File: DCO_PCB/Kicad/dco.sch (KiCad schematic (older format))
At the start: 0 parts

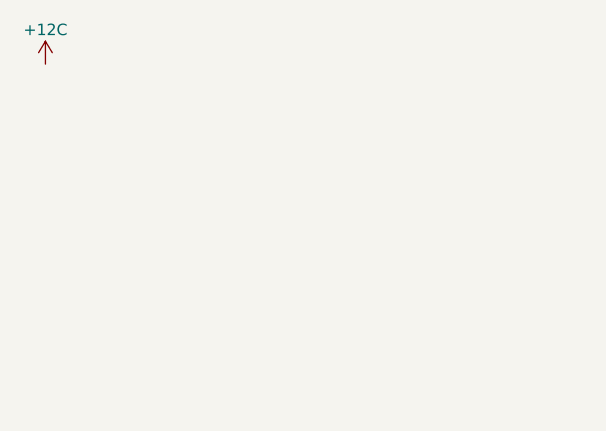
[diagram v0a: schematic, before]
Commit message: s-a adaugat gndd Signed-off-by: Botond Sandor Kirei <botond.kirei@bel.utcluj.ro>
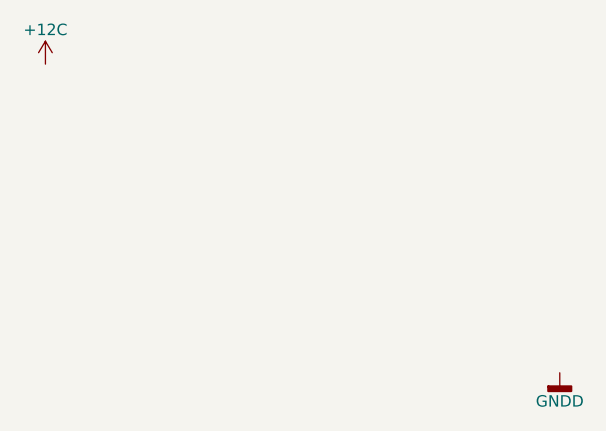
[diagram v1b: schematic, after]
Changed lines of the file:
@@
 LIBS:contrib
 LIBS:valves
+LIBS:dco-cache
 EELAYER 25 0
 EELAYER END
@@
 	1    0    0    -1
 $EndComp
+$Comp
+L GNDD #PWR?
+U 1 1 5AAFD078
+P 5650 3800
+F 0 "#PWR?" H 5650 3550 50  0001 C CNN
+F 1 "GNDD" H 5650 3675 50  0000 C CNN
+F 2 "" H 5650 3800 50  0001 C CNN
+F 3 "" H 5650 3800 50  0001 C CNN
+	1    5650 3800
+	1    0    0    -1
+$EndComp
